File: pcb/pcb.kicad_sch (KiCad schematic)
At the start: 20 parts, among them U1 K155ID1, U2 K155ID1, U3 K155ID1, U4 K155ID1

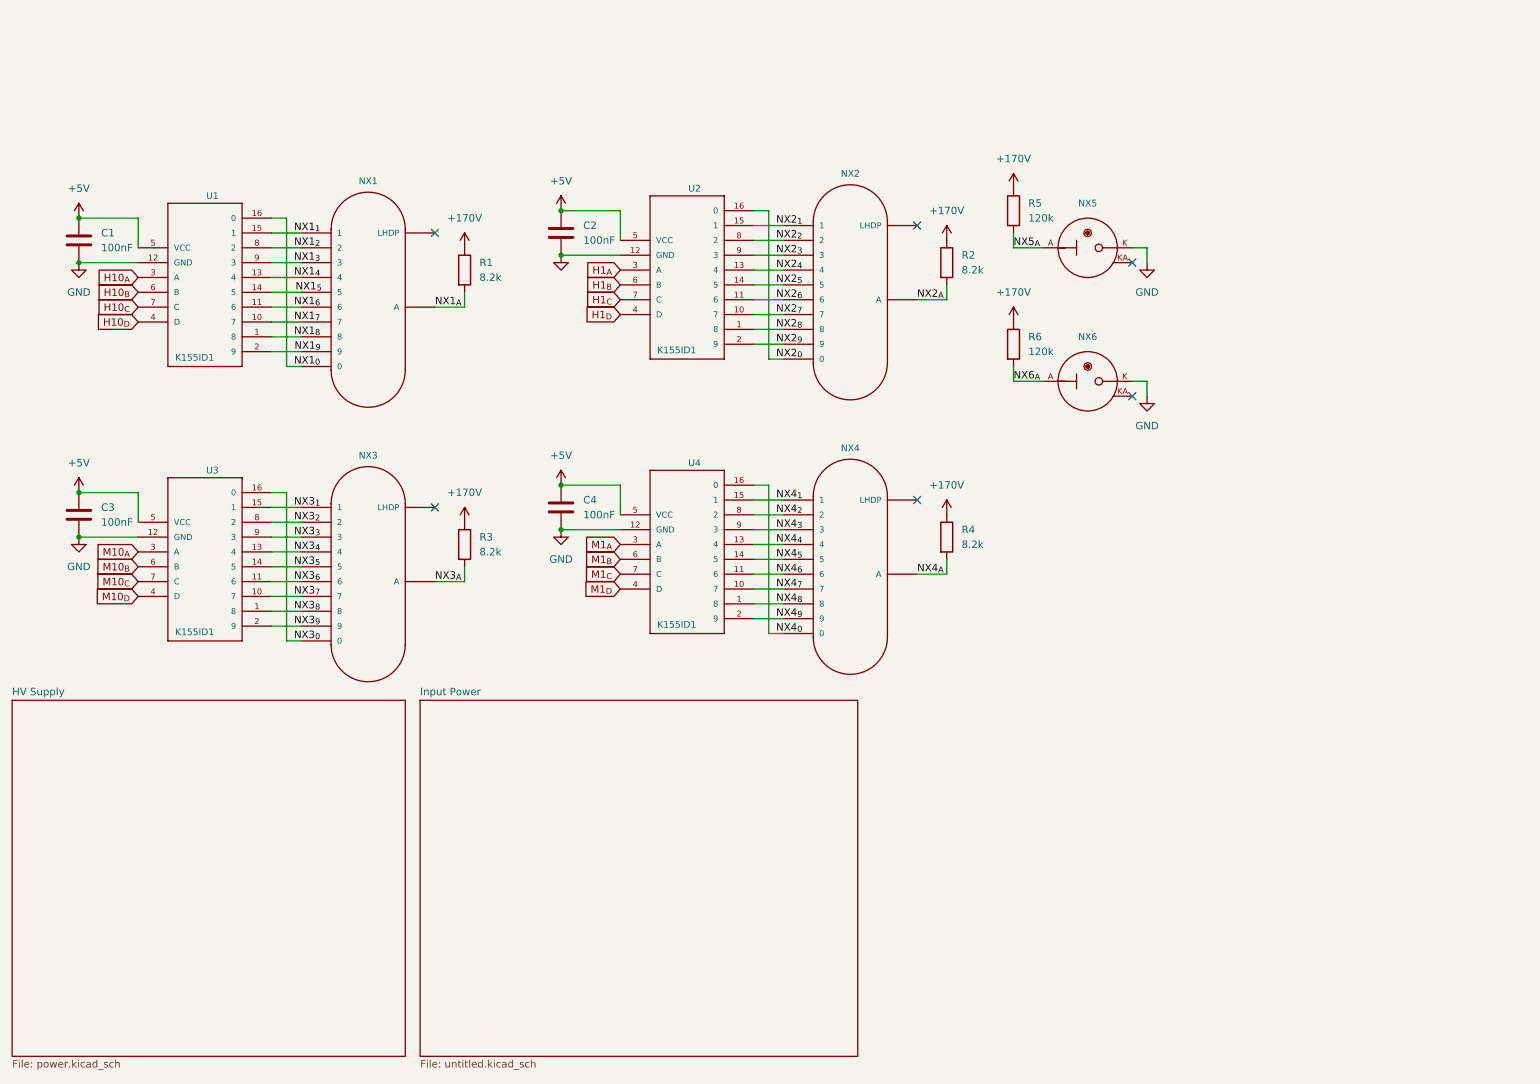
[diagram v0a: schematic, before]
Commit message: Add title and revision to schematic and board silkscreen, do a bit of tidying of the schematics
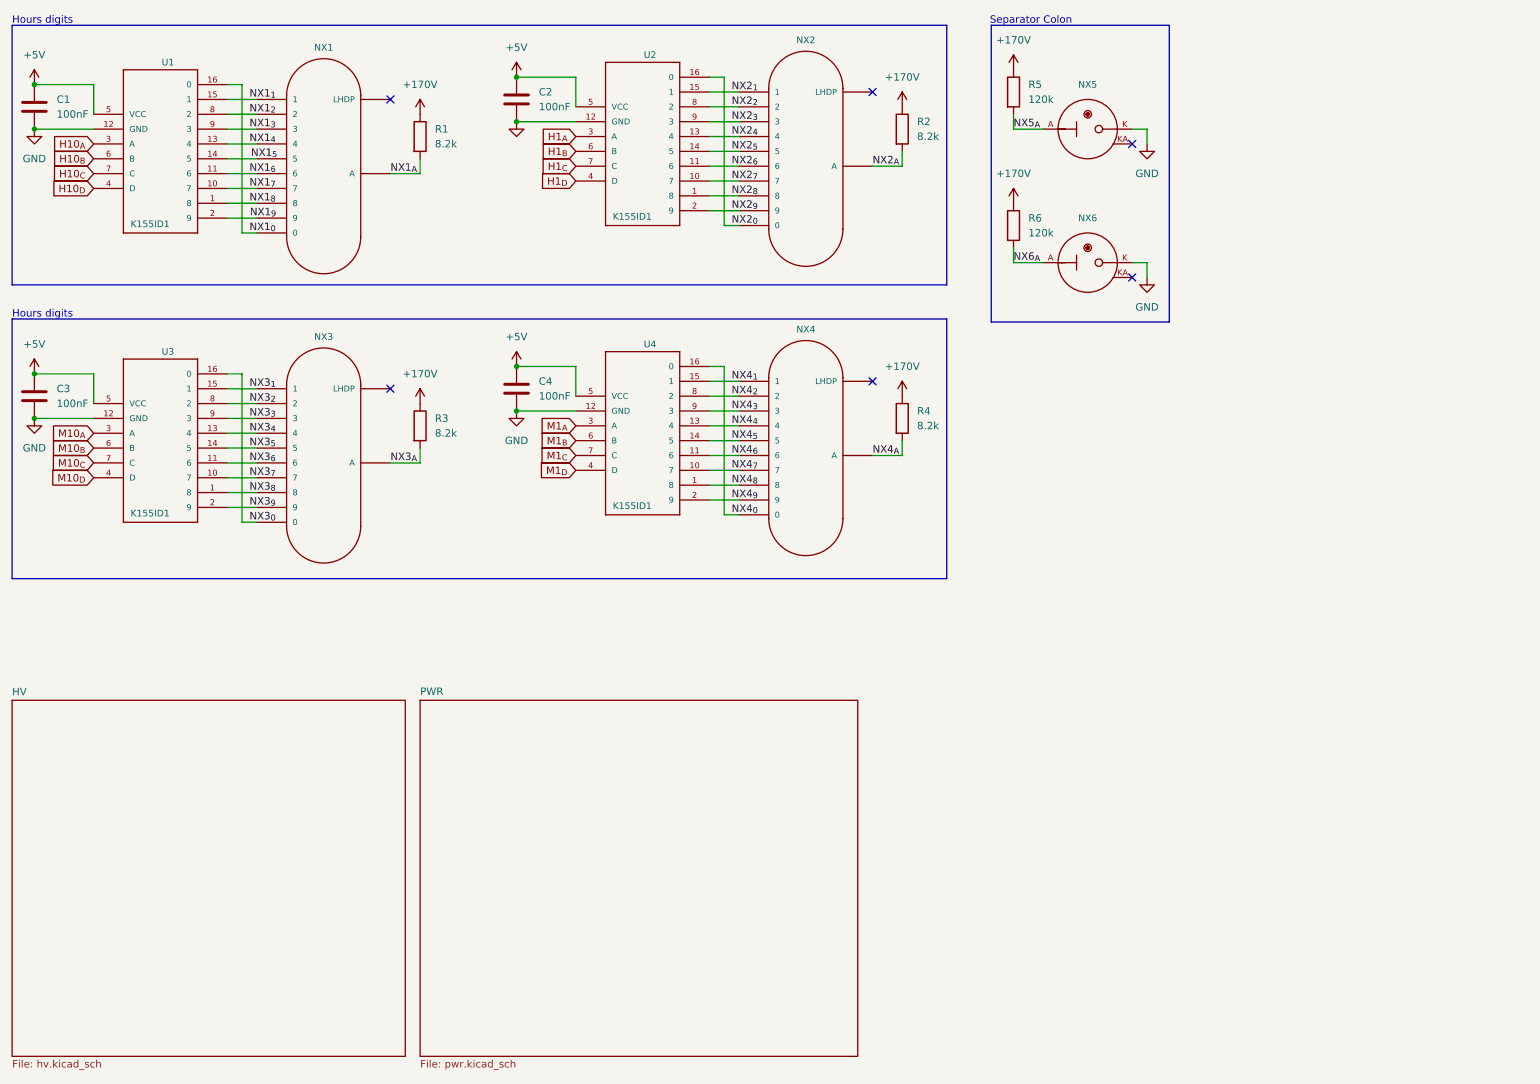
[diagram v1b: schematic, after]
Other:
- sheet HV Supply renamed HV
- sheet Input Power renamed PWR
- sheet HV: file power.kicad_sch -> hv.kicad_sch
- sheet PWR: file untitled.kicad_sch -> pwr.kicad_sch
- note added: "Hours digits"
- note added: "Separator Colon"
- title: (none) -> ${TITLE}
- moved on the sheet: C1, C2, C3, C4, NX1, NX2, NX3, NX4, NX5, NX6, R1, R2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

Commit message: Add ESP32, finish wiring. Rev A complete
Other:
- added sheet MCU (mcu.kicad_sch)
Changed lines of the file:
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@@
+		)
+	)
+	(sheet
+		(at 196.85 95.25)
+		(size 60.96 62.23)
+		(exclude_from_sim no)
+		(in_bom yes)
+		(on_board yes)
+		(dnp no)
+		(fields_autoplaced yes)
+		(stroke
+			(width 0.1524)
+			(type solid)
+		)
+		(fill
+			(color 0 0 0 0.0000)
+		)
+		(property "Sheetname" "MCU"
+			(at 196.85 94.5384 0)
+			(effects
+				(font
+					(size 1.27 1.27)
+				)
+				(justify left bottom)
+			)
+		)
+		(property "Sheetfile" "mcu.kicad_sch"
+			(at 196.85 158.0646 0)
+			(effects
+				(font
+					(size 1.27 1.27)
+				)
+				(justify left top)
+			)
+		)
+		(instances
+			(project "pcb"
+				(path "/7326c864-f0c7-4b19-9935-f5e4e9f8dcd3"
+					(page "5")
+				)
+			)
 		)
 	)

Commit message: Partial Rev B, committing before splitting projects
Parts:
- added H2, H3, H4, H5: MountingHole, MountingHole:MountingHole_3.2mm_M3_ISO7380, symbol Mechanical:MountingHole
- added J104: Conn_02x13_Counter_Clockwise, Connector_IDC:IDC-Header_2x13_P2.54mm_Vertical, symbol Connector_Generic:Conn_02x13_Odd_Even
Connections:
- net +5V: now also J104.12 (Pin_12), J104.14 (Pin_14), J104.16 (Pin_16)
- net GND: now also J104.11 (Pin_11), J104.13 (Pin_13), J104.15 (Pin_15)
- net H10_{A}: now also J104.23 (Pin_23)
- net H10_{B}: now also J104.24 (Pin_24)
- net H10_{C}: now also J104.26 (Pin_26)
- net H10_{D}: now also J104.25 (Pin_25)
- net H1_{A}: now also J104.21 (Pin_21)
- net H1_{B}: now also J104.19 (Pin_19)
- net H1_{C}: now also J104.20 (Pin_20)
- net H1_{D}: now also J104.22 (Pin_22)
- net M10_{A}: now also J104.8 (Pin_8)
- net M10_{B}: now also J104.6 (Pin_6)
- net M10_{C}: now also J104.5 (Pin_5)
- net M10_{D}: now also J104.7 (Pin_7)
- net M1_{A}: now also J104.2 (Pin_2)
- net M1_{B}: now also J104.1 (Pin_1)
- net M1_{C}: now also J104.3 (Pin_3)
- net M1_{D}: now also J104.4 (Pin_4)
